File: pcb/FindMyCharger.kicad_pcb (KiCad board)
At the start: 4 copper layers, 50 x 18 mm, 34 parts, among them J1 USB_C_Receptacle_USB2.0_14P, SW1 SKHLLDA010, U1 IP5353_I2C_AABC, U2 E104-BT5005A, U3 HT7533-1_C14289

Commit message: v2
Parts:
- moved TP2 22.9 mm to (100.0, 93.8)
- moved TP1 17.7 mm to (103.8, 93.8)
- moved BT1 15.3 mm to (120.8, 83.8), turned to 90 degrees
- moved TP4 3.76 mm to (114.0, 84.5)
- moved TP3 2.51 mm to (110.0, 83.5)
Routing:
- net Net-(BT1-+): track 19.0 -> 37.8 mm
- net Net-(U2-P0.21/RST): track 6.84 -> 0.00 mm
- net Net-(U2-SWCLK): track 11.2 -> 17.1 mm, vias 0 -> 2
- net Net-(U2-SWDIO): track 8.68 -> 12.5 mm
- net Net-(R1-Pad2): track 8.46 -> 9.17 mm
- net GND: track 22.8 -> 22.2 mm

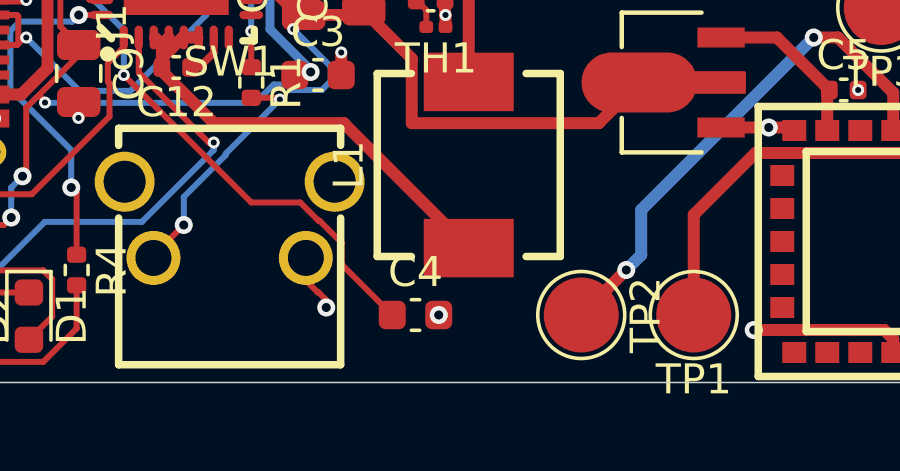
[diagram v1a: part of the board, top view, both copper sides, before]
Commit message: fix via directly on component
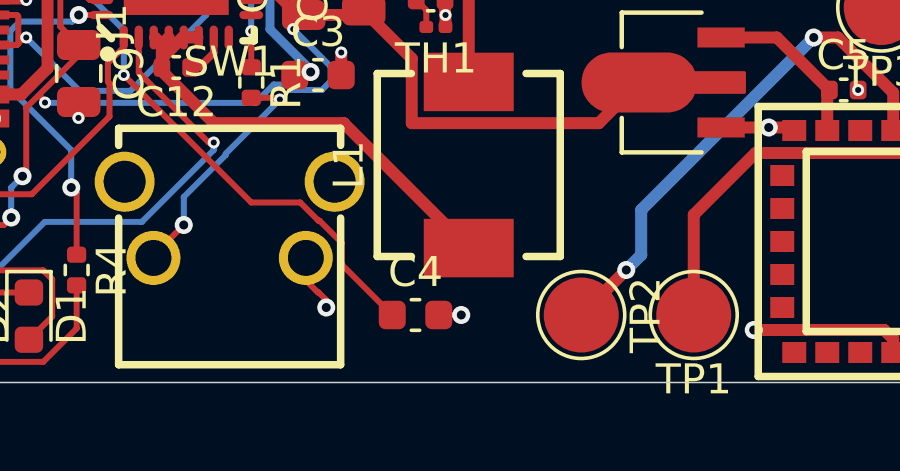
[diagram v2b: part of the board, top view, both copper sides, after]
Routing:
- net GND: track 22.2 -> 23.0 mm

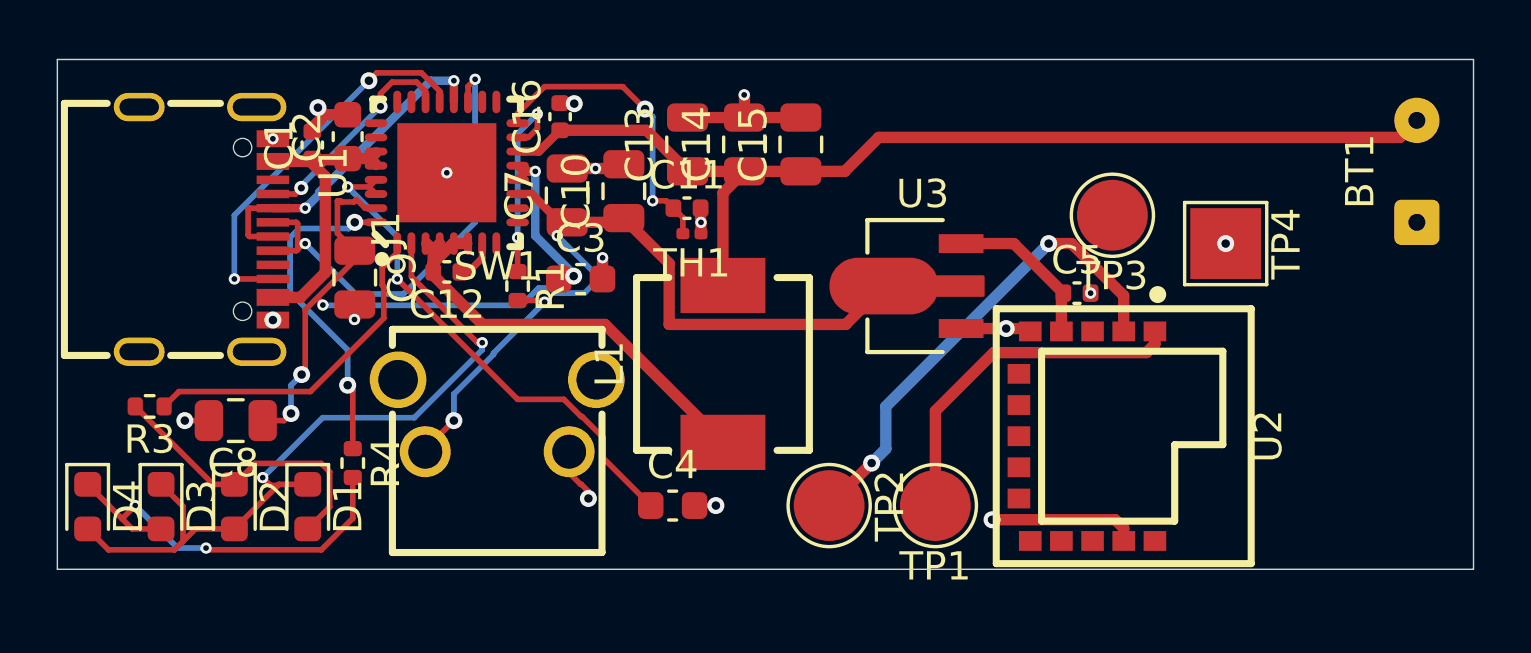
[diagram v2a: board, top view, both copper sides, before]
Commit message: forgot to connect nRST
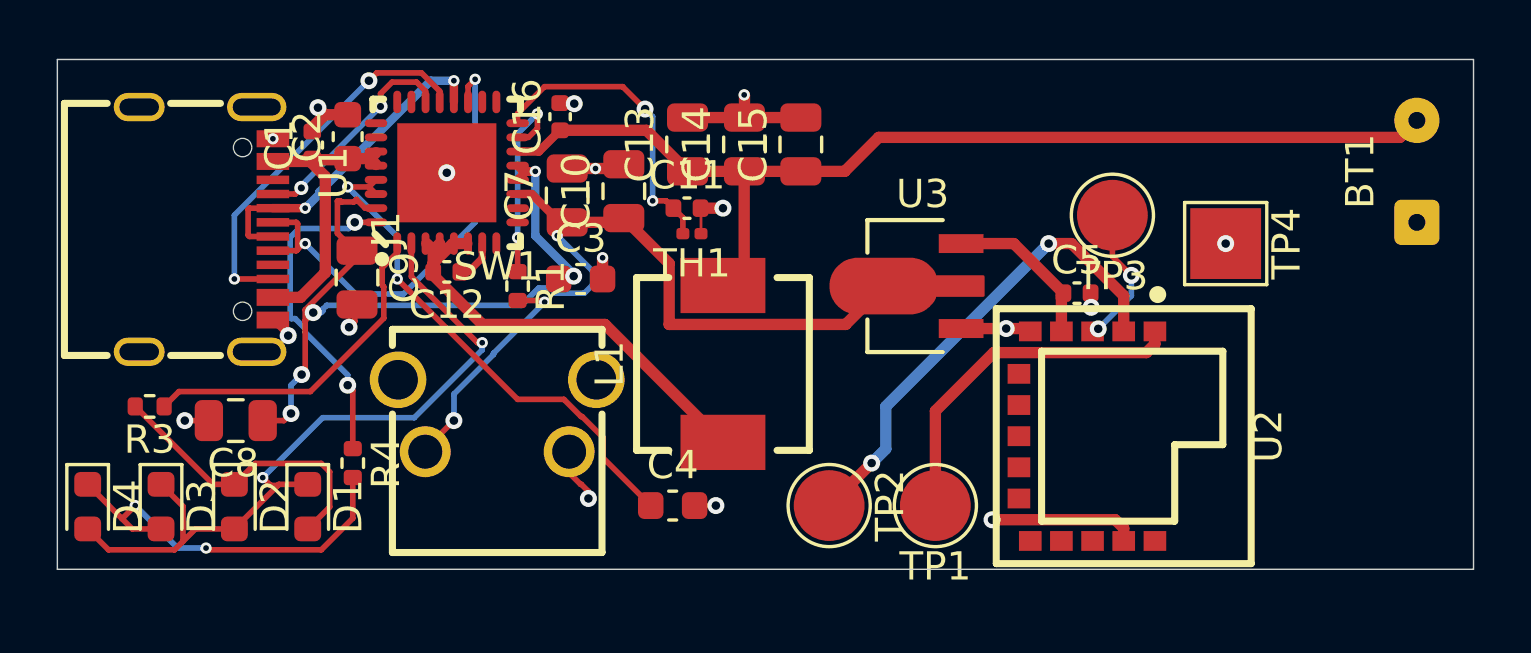
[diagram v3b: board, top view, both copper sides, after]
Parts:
- moved C9 0.08 mm to (83.3, 85.7)
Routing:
- net Net-(U2-P0.21/RST): track 0.00 -> 5.01 mm, vias 0 -> 2
- net GND: track 23.0 -> 25.4 mm
- net Net-(U3-Vin): track 41.2 -> 41.9 mm

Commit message: fixed drc
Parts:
- added 3V3: 3V3, TestPoint:TestPoint_Pad_D2.5mm, F.Cu at (106.8, 82.0)
- moved C13 23.0 mm to (118.0, 80.9), turned to -90 degrees
- moved C14 18.7 mm to (115.8, 80.9), turned to -90 degrees
- moved C15 14.5 mm to (113.5, 80.9), turned to -90 degrees
- moved U3 3.23 mm to (102.1, 83.0)
- moved C10 0.65 mm to (93.4, 82.7)
- moved C12 0.58 mm to (87.0, 85.8)
- moved C11 0.54 mm to (95.5, 83.2)
- moved C7 0.51 mm to (91.2, 82.7)
- moved U1 0.50 mm to (87.0, 82.0)
- moved R1 0.26 mm to (89.0, 86.3)
- moved TH1 0.25 mm to (95.4, 84.2)
- moved C16 0.25 mm to (90.8, 80.0)
- renumbered BT1 to BAT+, TP2 to CLK, TP1 to DIO, TP4 to GND, TP3 to RST
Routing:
- net Net-(U1-DPC): track 16.8 -> 27.5 mm
- net GND: track 25.4 -> 34.4 mm, vias 17 -> 15
- net Net-(D1-K): track 26.5 -> 34.7 mm
- net Net-(BT1-+): track 37.8 -> 43.7 mm
- net Net-(U1-LED2): track 11.9 -> 17.4 mm, vias 0 -> 4
- net Net-(J1-CC1): track 7.85 -> 13.2 mm, vias 2 -> 0
- net Net-(J1-CC2): track 13.6 -> 17.8 mm, vias 2 -> 0
- net +3V3: track 5.71 -> 9.69 mm
- net Net-(C1-Pad1): track 10.6 -> 12.8 mm
- net Net-(C12-Pad2): track 16.0 -> 18.2 mm
- net Net-(U3-Vin): track 41.9 -> 40.5 mm, vias 4 -> 2
- net Net-(C3-Pad1): track 6.29 -> 5.05 mm
- net Net-(U1-KEY): track 7.20 -> 8.16 mm
- net Net-(U1-LED1): track 11.7 -> 12.2 mm
- net Net-(C4-Pad1): track 18.1 -> 18.6 mm, vias 2 -> 4
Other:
- board text added: "GND"
